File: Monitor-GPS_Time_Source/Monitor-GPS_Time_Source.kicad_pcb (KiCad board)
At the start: 2 copper layers, 21.4 x 26.5 mm, 17 parts, among them J1 2x5, 1.27mm, J2 1x10, 2.54mm, J3 1x10, 2.54mm, J4 1x3, 2.54mm, SW2 ALPS SKRK, U1 MSPM0C1105, U2 BL8565

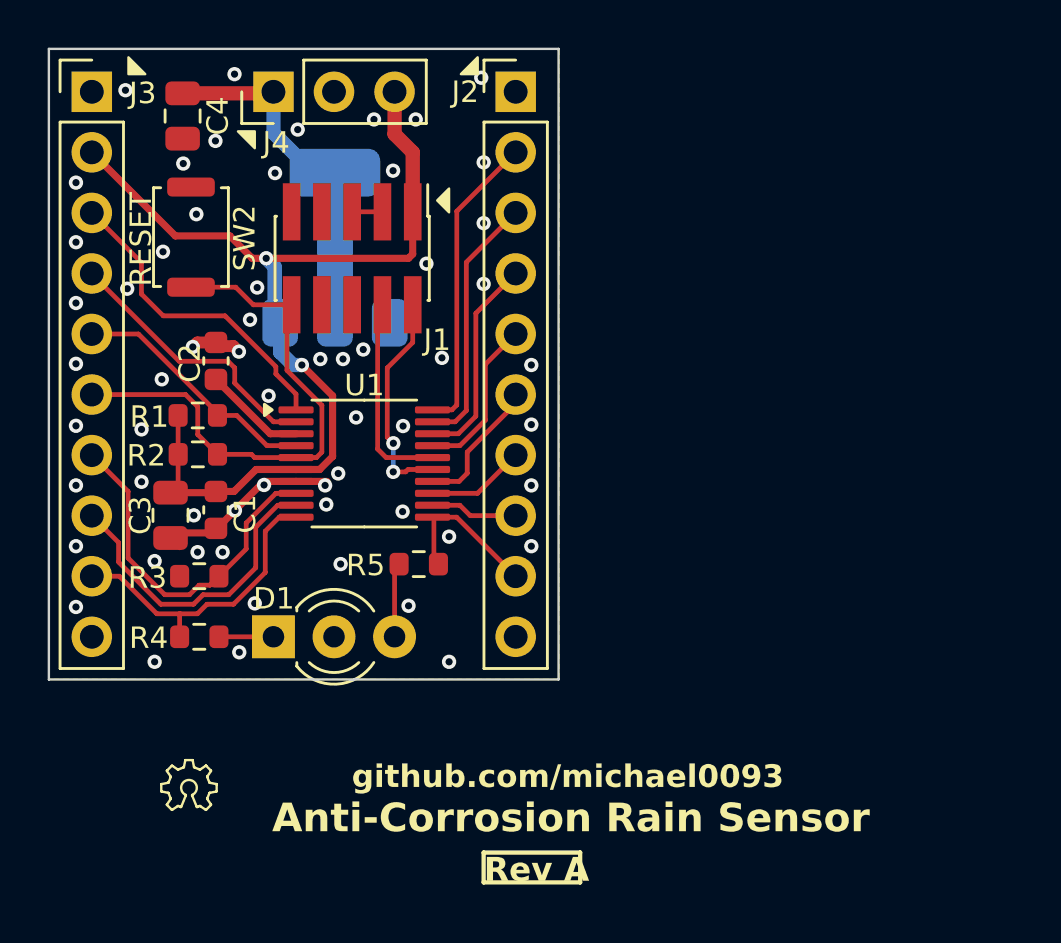
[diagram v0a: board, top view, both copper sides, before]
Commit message: Add silkscreen text. Update sch to support MSPM0C110x
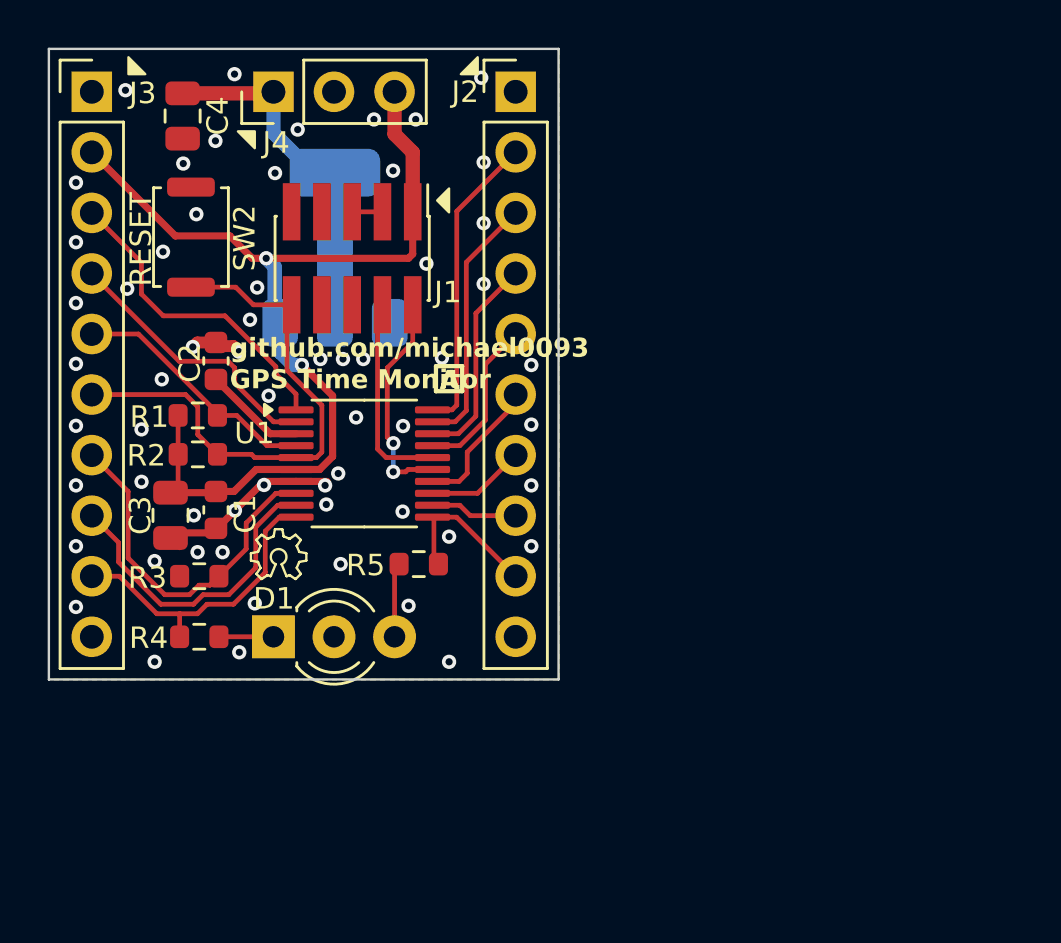
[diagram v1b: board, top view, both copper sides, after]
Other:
- board text added: "A"
- board text added: "GPS Time Monitor"
- board text removed: "Anti-Corrosion Rain Sensor"
- board text removed: "Rev A"

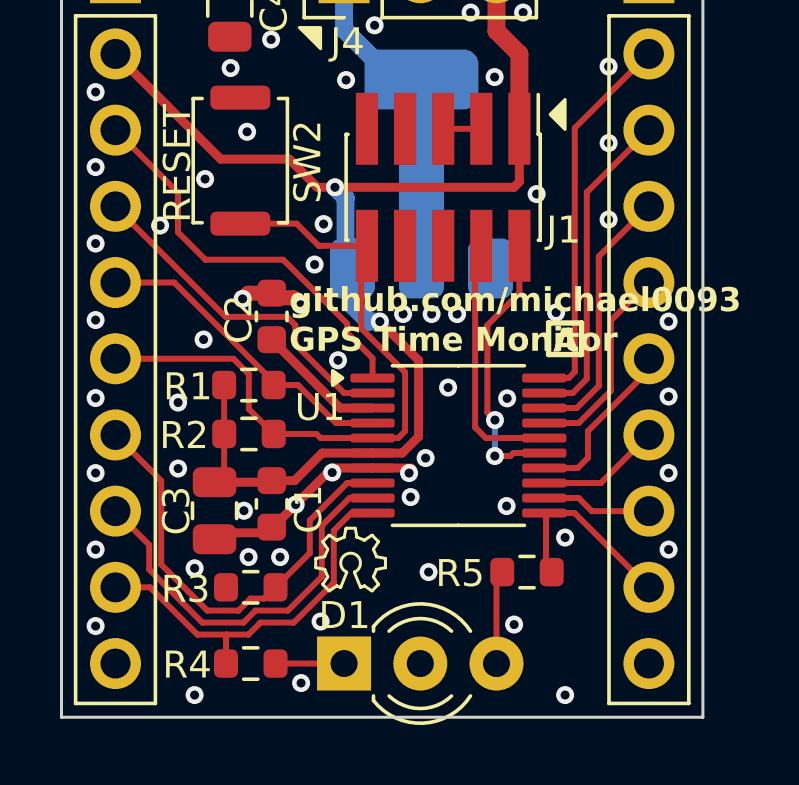
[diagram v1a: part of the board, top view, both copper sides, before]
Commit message: Updated silkscreen for MSPM0. Finished DRC edits
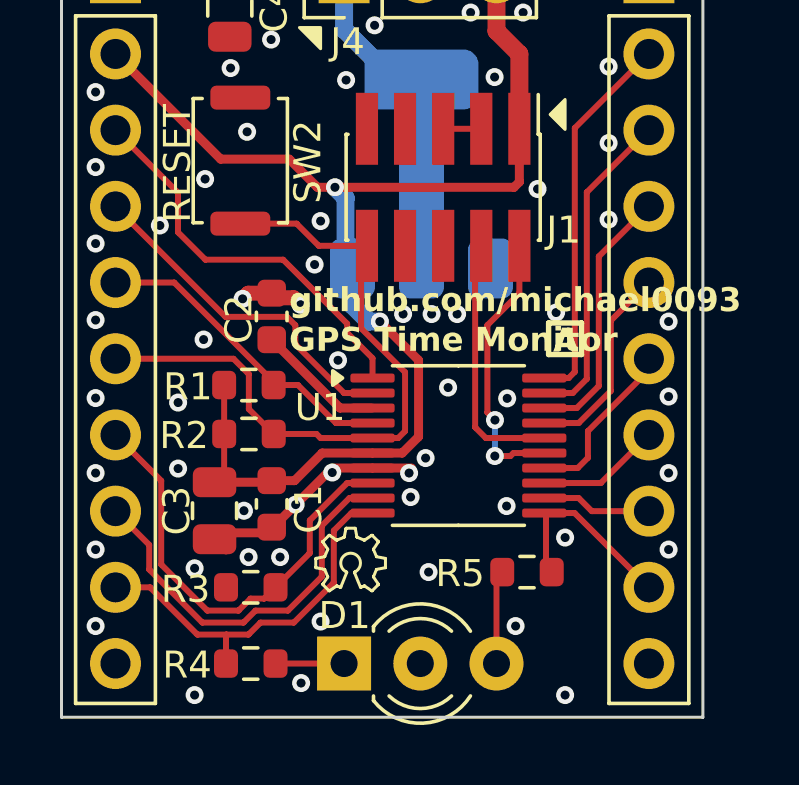
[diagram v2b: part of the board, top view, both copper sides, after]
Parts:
- J1: value 2x5, 1.27mm -> Conn 2x5, 1.27mm
- J2, J3: value 1x10, 2.54mm -> Conn 1x10, 2.54mm
- J4: value 1x3, 2.54mm -> Conn 1x3, 2.54mm
- SW2: value ALPS SKRK -> SW_Push
- U1: value MSPM0C1105 -> MSPM0L110x
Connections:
- net /I2C0_SCL renamed /PA1/I2C0_SCL
- net /I2C0_SDA renamed /PA0/I2C0_SDA
- net /LED-GRN renamed /PA6/LED-GRN
- net /LED-RED renamed /PA11/LED-RED
- net /PA23 renamed /PA23/UART0_TX
- net /PA26 renamed /PA26/UART0_RX
- net /UART0_RX renamed /PA18
- net /UART0_TX renamed /PA17
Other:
- board text added: "GND PA25 PA24 PA23 PA22 PA18 PA17 PA16"
- board text added: "U0RX"
- board text added: "U0TX"
- board text removed: "GND PA25 PA24 PA23 PA22 PA18/U0RX PA17/U0TX PA16"
